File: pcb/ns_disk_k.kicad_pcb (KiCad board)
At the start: 2 copper layers, 76.2 x 78 mm, 17 parts, among them J2 OLED Display, J3 Buttons, J4 MICRO-SD-CARD, P1 northstar card edge, U1 TXS0108EPW, U2 TXS0108EPW, U3 AMS1117-3.3

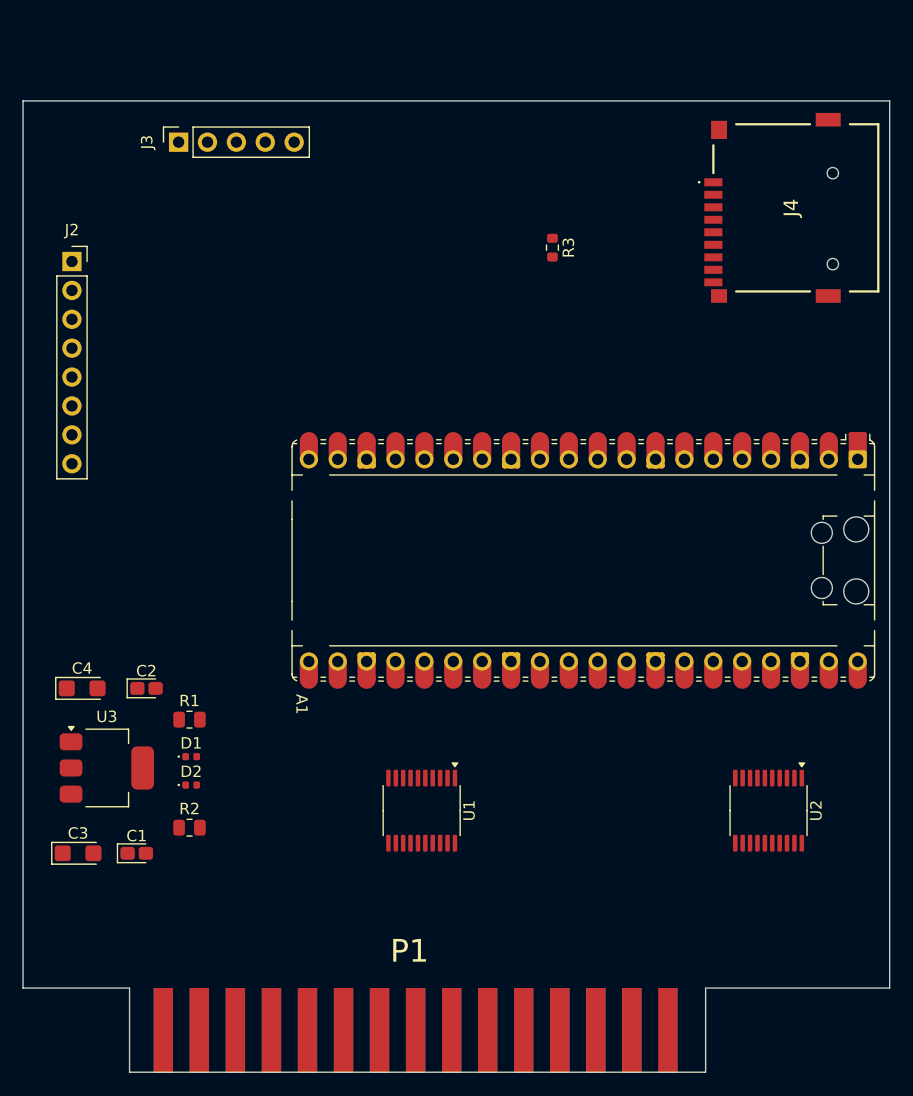
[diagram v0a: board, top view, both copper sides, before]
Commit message: - Fix /ID REQ - Re-add /SELECT - A3 remains on level shifter no on pi-pico - Added header pins for power - Added holes to pcb
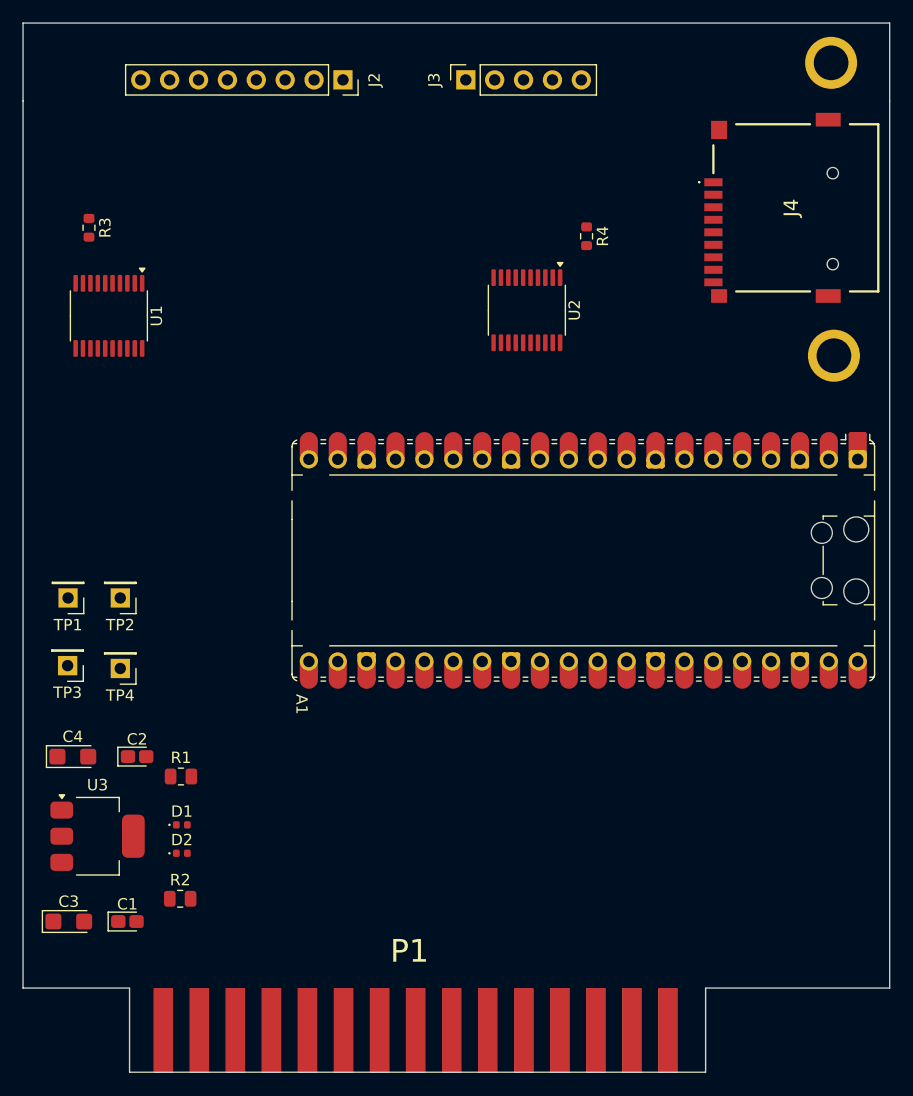
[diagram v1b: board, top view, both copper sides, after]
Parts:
- added ?: , , F.Cu at (179.8, 68.8)
- added ?: , , F.Cu at (180.0, 94.5)
- added R4: 2.2k, Resistor_SMD:R_0603_1608Metric, F.Cu at (158.2, 84.0)
- added TP1: +3.3v, Connector_PinHeader_2.54mm:PinHeader_1x01_P2.54mm_Vertical, F.Cu at (112.7, 115.8)
- added TP2: 5v, Connector_PinHeader_2.54mm:PinHeader_1x01_P2.54mm_Vertical, F.Cu at (117.2, 115.8)
- added TP3: gnd, Connector_PinHeader_2.54mm:PinHeader_1x01_P2.54mm_Vertical, F.Cu at (112.6, 121.8)
- added TP4: gnd, Connector_PinHeader_2.54mm:PinHeader_1x01_P2.54mm_Vertical, F.Cu at (117.2, 122.0)
- moved U1 51.5 mm to (116.2, 91.0)
- moved U2 48.9 mm to (153.0, 90.5)
- moved R3 40.8 mm to (114.5, 83.2)
- moved J2 28.7 mm to (136.8, 70.2), turned to -90 degrees
- moved J3 25.8 mm to (147.6, 70.2)
- moved R2 6.30 mm to (122.5, 142.2)
- moved C1 6.06 mm to (117.9, 144.2)
- moved C3 6.06 mm to (112.7, 144.2)
- moved C2 6.06 mm to (118.7, 129.8)
- moved C4 6.06 mm to (113.1, 129.8)
- moved D1 6.06 mm to (122.7, 135.8)
- moved D2 6.06 mm to (122.7, 138.2)
- moved U3 6.06 mm to (115.2, 136.8)
- moved R1 5.06 mm to (122.6, 131.5)
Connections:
- A1 pad 13: GND -> /ID REQ
- A1 pad 18: GND -> /ID REQ
- A1 pad 23: GND -> /ID REQ
- A1 pad 28: GND -> /ID REQ
- A1 pad 3: GND -> /ID REQ
- A1 pad 36: OE_ACT -> unconnected-(A1-3V3-Pad36)
- A1 pad 38: GND -> /ID REQ
- A1 pad 8: GND -> /ID REQ
- C1 pad 2: GND -> /ID REQ
- C2 pad 2: GND -> /ID REQ
- C3 pad 2: GND -> /ID REQ
- C4 pad 2: GND -> /ID REQ
- J2 pad 1: GND -> /ID REQ
- J3 pad 5: GND -> /ID REQ
- J4 pad 6: GND -> /ID REQ
- J4 pad G1: GND -> /ID REQ
- P1 pad 1: GND -> /ID REQ
- P1 pad 12: GND -> /ID REQ
- P1 pad 21: GND -> /ID REQ
- P1 pad 30: GND -> /ID REQ
- R1 pad 1: GND -> /ID REQ
- R2 pad 2: GND -> /ID REQ
- R3 pad 2: GND -> /ID REQ
- U1 pad 11: GND -> /ID REQ
- U1 pad 12: /IDREQ -> /ID REQ
- U2 pad 11: GND -> /ID REQ
- U3 pad 1: GND -> /ID REQ
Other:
- board size 76.2 x 78 mm -> 76.2 x 84.8 mm
